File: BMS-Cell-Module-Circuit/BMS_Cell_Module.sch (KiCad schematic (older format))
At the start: 46 parts, among them J1 Conn_01x04_Female, J2 Conn_01x04_Female, J3 Conn_01x02_Male, M1 SI2312BDS-T1-E3, U1 MCP1703A-3302_SOT223, U2 ADUM1250ARZ, U3 ATTINY85-20SU

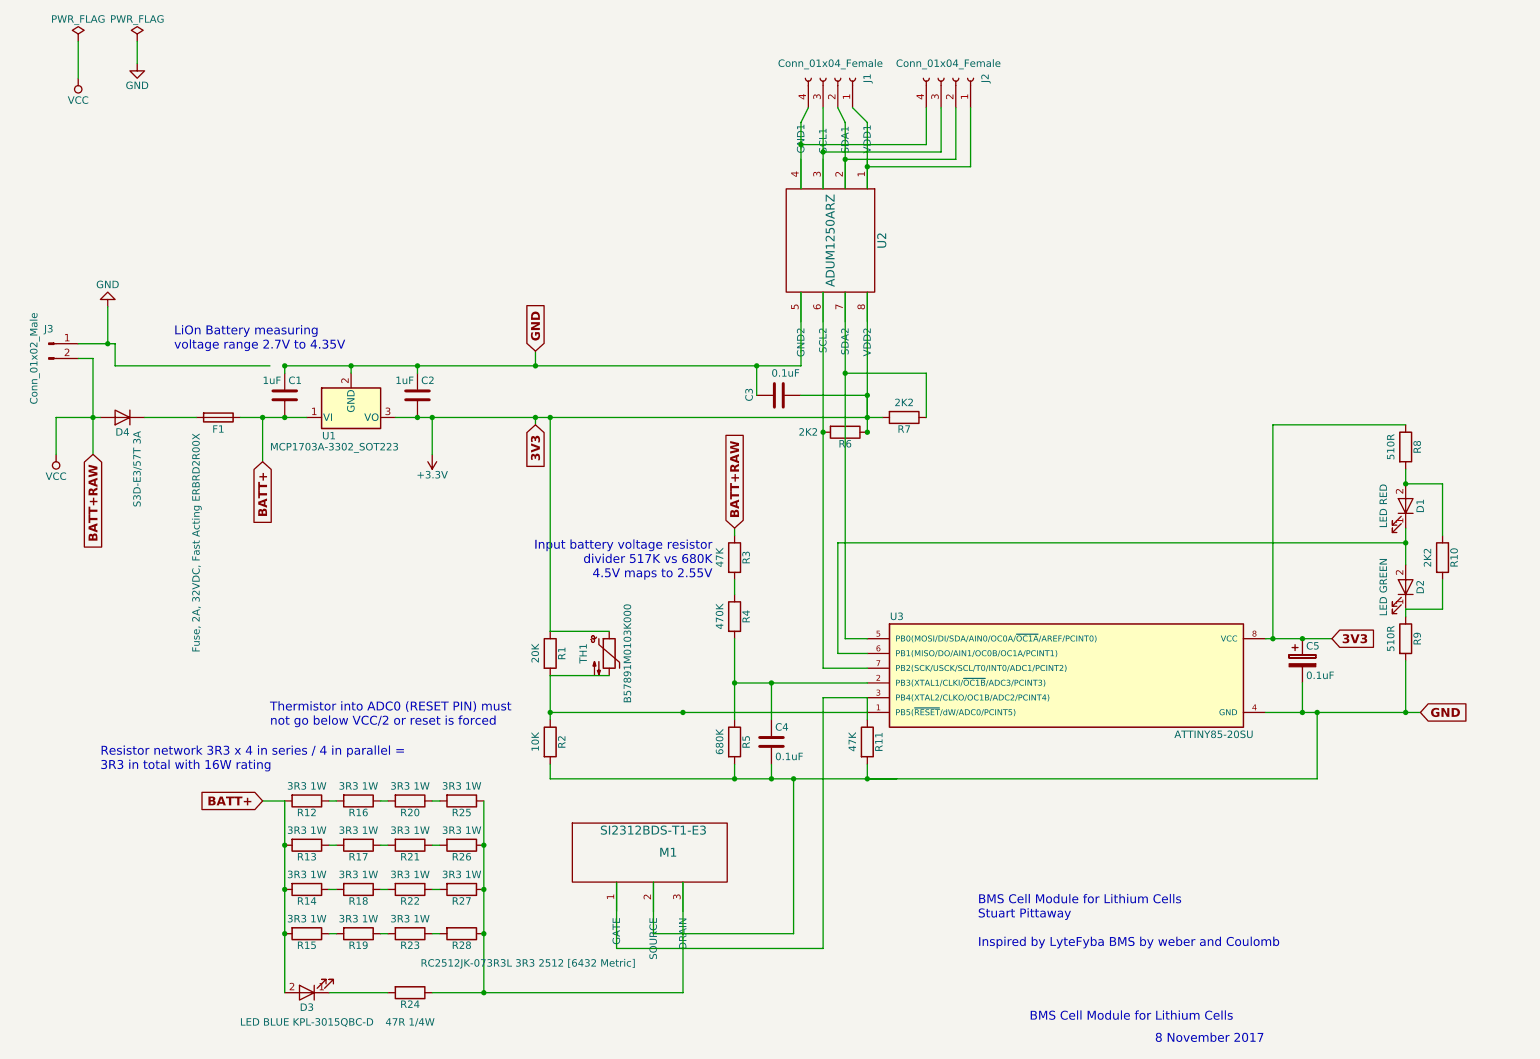
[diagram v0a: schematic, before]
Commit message: Started work on PCB
DONT USE THIS PCB FOR PRODUCTION!
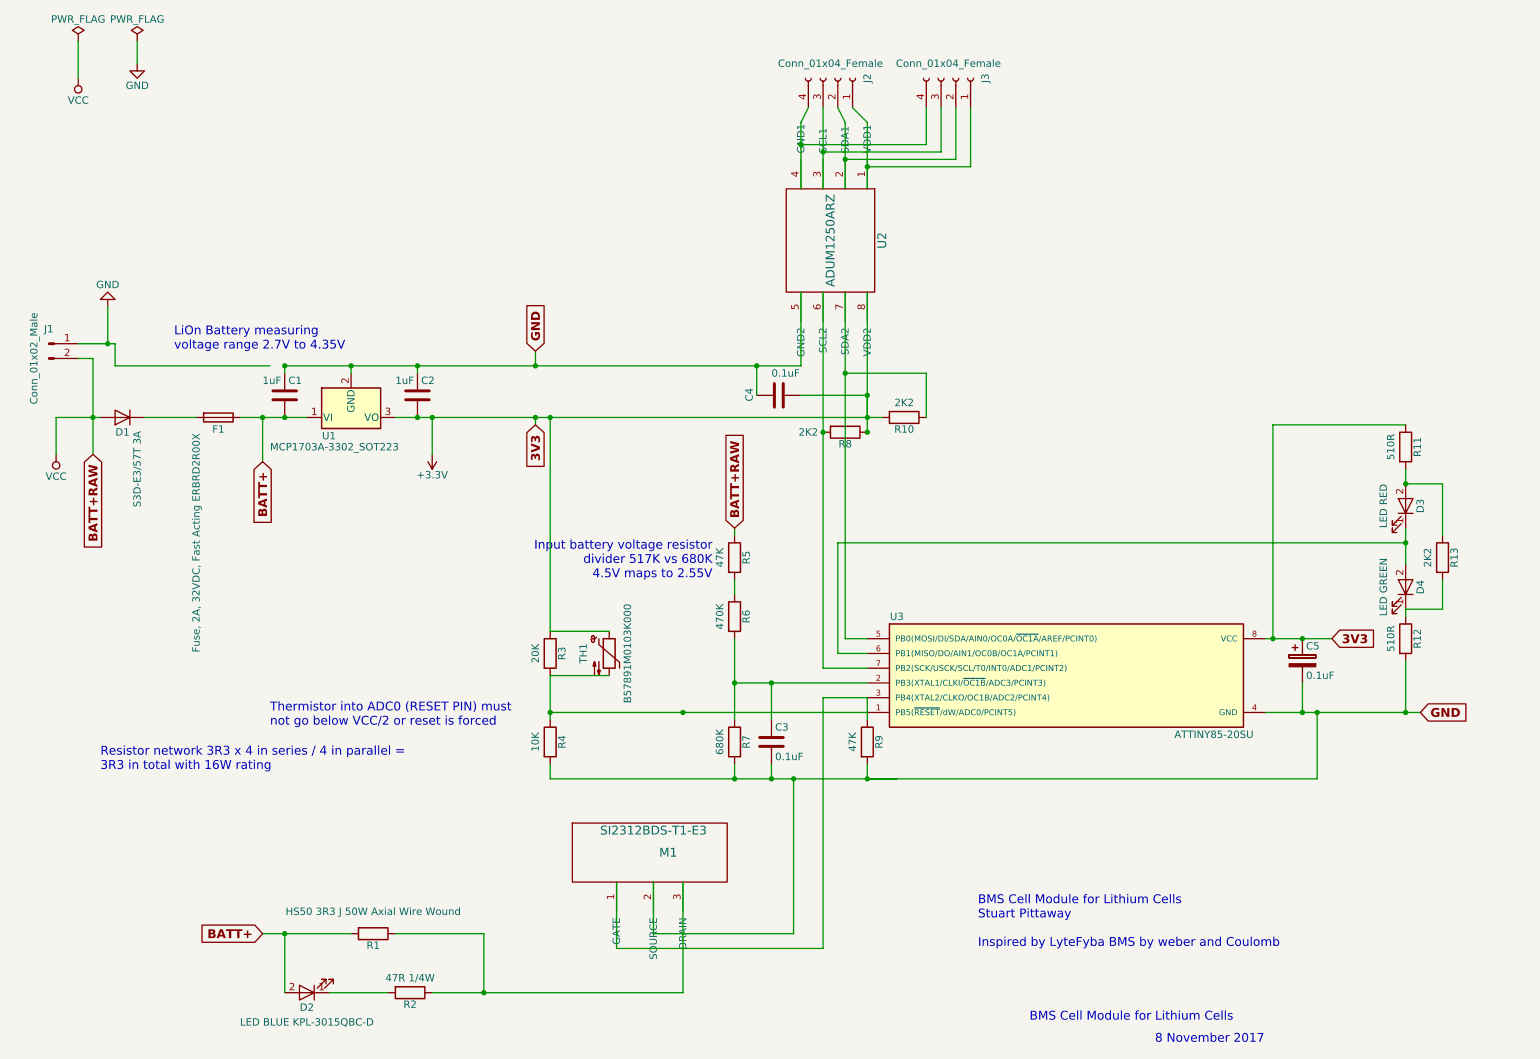
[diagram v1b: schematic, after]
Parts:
- removed R12, R13, R14, R15, R16, R17, R18, R19, R20, R21, R22, R23, R25, R26, R27: 3R3 1W, Resistors_SMD:R_2512_HandSoldering, symbol R
- removed R28: RC2512JK-073R3L 3R3 2512 [6432 Metric], Resistors_SMD:R_2512_HandSoldering, symbol R
- added R1: HS50 3R3 J 50W Axial Wire Wound, Resistors_THT:R_Axial_Power_L60.0mm_W14.0mm_P71.12mm, symbol R
- TH1: footprint Pin_Headers:Pin_Header_Straight_1x02_Pitch2.54mm -> Resistors_THT:R_Axial_DIN0204_L3.6mm_D1.6mm_P2.54mm_Vertical
- renumbered C4 to C3, C3 to C4, D4 to D1, D3 to D2, D1 to D3, D2 to D4, J3 to J1, J1 to J2, J2 to J3, R7 to R10, R8 to R11, R9 to R12, R10 to R13, R24 to R2, R1 to R3, R2 to R4, R3 to R5, R4 to R6, R5 to R7, R6 to R8, R11 to R9
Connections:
- net BATT+: now also R1.2
- net at M1.3 (DRAIN), R2.1: now also R1.1

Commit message: Split board into two sections
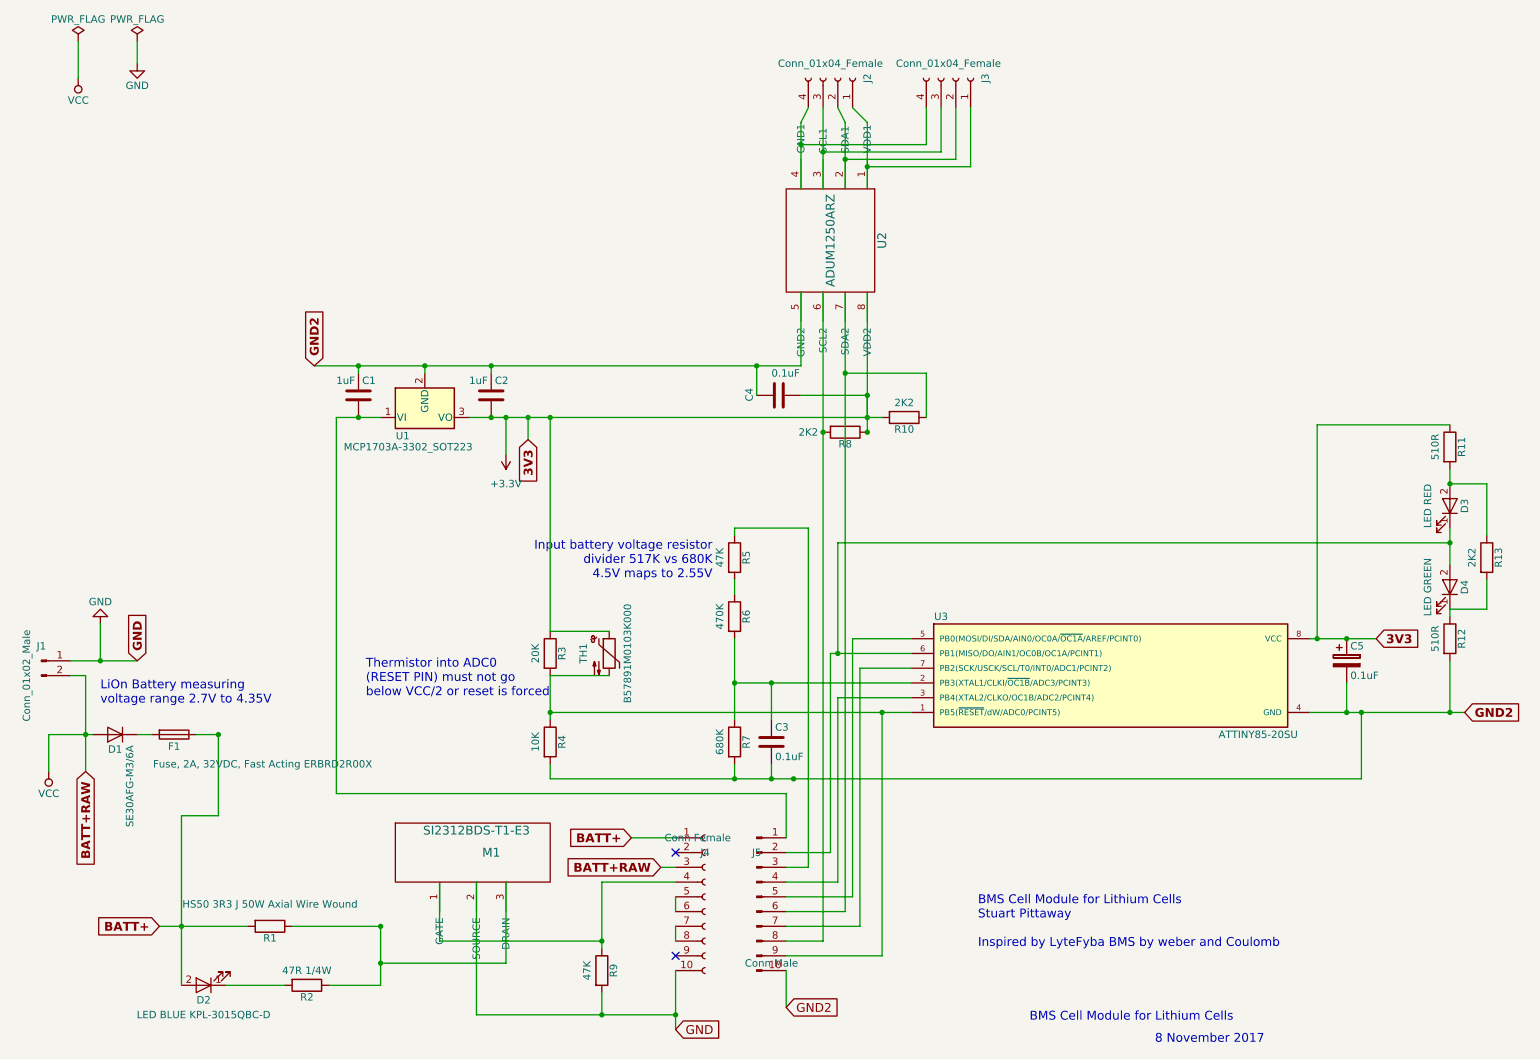
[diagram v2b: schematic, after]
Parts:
- added J4: Conn Female, Socket_Strips:Socket_Strip_Angled_1x10_Pitch2.54mm, symbol Conn_01x10_Female
- added J5: Conn Male, Pin_Headers:Pin_Header_Angled_1x10_Pitch2.54mm, symbol Conn_01x10_Male
- D1: value S3D-E3/57T 3A -> SE30AFG-M3/6A; footprint Diodes_SMD:D_SMC_Handsoldering -> Diodes_SMD:D_SMA
- D2, D3, D4: footprint LEDs:LED_0603_HandSoldering -> LEDs:LED_1206_HandSoldering
- J1: footprint Connectors_JST:JST_VH_B2PS-VH_2x2x3.96mm_Horizontal -> Connectors_JST:JST_EH_S02B-EH_02x2.50mm_Angled
- R1: footprint Resistors_THT:R_Axial_Power_L60.0mm_W14.0mm_P71.12mm -> Resistors_THT:R_Axial_Power_L50.0mm_W9.0mm_P60.96mm
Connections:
- net BATT+: now also J4.1 (Pin_1); no longer C1.2, U1.1 (VI)
- net GND: now also J4.10 (Pin_10); no longer C1.1, C2.1, C3.2, C4.2, C5.2, R12.2, R4.2, R7.2, U1.2 (GND), U2.5 (GND2), U3.4 (GND)
- net VCC: now also J4.3 (Pin_3); no longer R5.1
- net at R3.2, R4.1, TH1.2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: now also J5.9 (Pin_9)
- net at M1.1 (GATE), R9.1: now also J4.4 (Pin_4); no longer U3.3 (PB4(XTAL2/CLKO/OC1B/ADC2/PCINT4))
- net at R10.1, U2.7 (SDA2): now also J5.6 (Pin_6); no longer U3.5 (PB0(MOSI/DI/SDA/AIN0/OC0A/~OC1A~/AREF/PCINT0))
- net at D3.1 (K), D4.2 (A), U3.6 (PB1(MISO/DO/AIN1/OC0B/OC1A/PCINT1)): now also J5.2 (Pin_2)
- net at R8.2, U2.6 (SCL2): now also J5.8 (Pin_8); no longer U3.7 (PB2(SCK/USCK/SCL/T0/INT0/ADC1/PCINT2))
- new net: J5.4 (Pin_4), U3.3 (PB4(XTAL2/CLKO/OC1B/ADC2/PCINT4))
- new net: J5.5 (Pin_5), U3.5 (PB0(MOSI/DI/SDA/AIN0/OC0A/~OC1A~/AREF/PCINT0))
- new net: J5.7 (Pin_7), U3.7 (PB2(SCK/USCK/SCL/T0/INT0/ADC1/PCINT2))
- new net: C1.2, J5.1 (Pin_1), U1.1 (VI)
- new net: J5.3 (Pin_3), R5.1
- new net: J4.5 (Pin_5), J4.6 (Pin_6)
- new net: J4.7 (Pin_7), J4.8 (Pin_8)
- new net GND2: C1.1, C2.1, C3.2, C4.2, C5.2, J5.10 (Pin_10), R12.2, R4.2, R7.2, U1.2 (GND), U2.5 (GND2), U3.4 (GND)
- no-connect marks 0 -> 2
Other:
- note added: "Thermistor into ADC0 \n(RESET PIN) must not go \nbelow VCC/2 or reset is forced"
- note removed: "Resistor network 3R3 x 4 in series / 4 in parallel = \n3R3 in total with 16W rating"
- note removed: "Thermistor into ADC0 (RESET PIN) must \nnot go below VCC/2 or reset is forced"
- moved on the sheet: C1, C2, C5, D1, D2, D3, D4, F1, J1, M1, R1, R11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

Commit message: All pins connected on PCB
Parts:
- added TP1: TEST, Connectors:PINTST, symbol TEST
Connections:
- net at C3.1, R6.2, R7.1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: now also TP1.1
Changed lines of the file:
@@
 $EndComp
 $Comp
-L GND #PWR01
+L GND #PWR3
 U 1 1 5A022A52
 P 1150 4800
-F 0 "#PWR01" H 1150 4550 50  0001 C CNN
+F 0 "#PWR3" H 1150 4550 50  0001 C CNN
 F 1 "GND" H 1150 4650 50  0000 C CNN
 F 2 "" H 1150 4800 50  0001 C CNN
@@
 $EndComp
 $Comp
-L +3.3V #PWR02
+L +3.3V #PWR5
 U 1 1 5A022FFB
 P 3900 3650
-F 0 "#PWR02" H 3900 3500 50  0001 C CNN
+F 0 "#PWR5" H 3900 3500 50  0001 C CNN
 F 1 "+3.3V" H 3900 3850 50  0000 C CNN
 F 2 "" H 3900 3650 50  0001 C CNN
@@
 $EndComp
 $Comp
-L PWR_FLAG #FLG03
+L PWR_FLAG #FLG1
 U 1 1 5A024000
 P 1000 850
-F 0 "#FLG03" H 1000 925 50  0001 C CNN
+F 0 "#FLG1" H 1000 925 50  0001 C CNN
 F 1 "PWR_FLAG" H 1000 1000 50  0000 C CNN
 F 2 "" H 1000 850 50  0001 C CNN
@@
 $EndComp
 $Comp
-L PWR_FLAG #FLG04
+L PWR_FLAG #FLG2
 U 1 1 5A02407E
 P 1400 850
-F 0 "#FLG04" H 1400 925 50  0001 C CNN
+F 0 "#FLG2" H 1400 925 50  0001 C CNN
 F 1 "PWR_FLAG" H 1400 1000 50  0000 C CNN
 F 2 "" H 1400 850 50  0001 C CNN
@@
 $EndComp
 $Comp
-L VCC #PWR05
+L VCC #PWR2
 U 1 1 5A0240F2
 P 1000 1100
-F 0 "#PWR05" H 1000 950 50  0001 C CNN
+F 0 "#PWR2" H 1000 950 50  0001 C CNN
 F 1 "VCC" H 1000 1250 50  0000 C CNN
 F 2 "" H 1000 1100 50  0001 C CNN
@@
 $EndComp
 $Comp
-L GND #PWR06
+L GND #PWR4
 U 1 1 5A024136
 P 1400 1000
-F 0 "#PWR06" H 1400 750 50  0001 C CNN
+F 0 "#PWR4" H 1400 750 50  0001 C CNN
 F 1 "GND" H 1400 850 50  0000 C CNN
 F 2 "" H 1400 1000 50  0001 C CNN
@@
 $EndComp
 $Comp
-L VCC #PWR07
+L VCC #PWR1
 U 1 1 5A04296E
 P 800 5800
-F 0 "#PWR07" H 800 5650 50  0001 C CNN
+F 0 "#PWR1" H 800 5650 50  0001 C CNN
 F 1 "VCC" H 800 5950 50  0000 C CNN
 F 2 "" H 800 5800 50  0001 C CNN
@@
 	2600 3050 5900 3050
 Wire Wire Line
-	5450 5200 6650 5200
+	5150 5200 6650 5200
 Wire Wire Line
 	1150 4800 1150 5050
@@
 	4550 7300 4550 7450
 Connection ~ 4550 7450
+$Comp
+L TEST TP1
+U 1 1 5A0A2523
+P 5150 5200
+F 0 "TP1" H 5150 5500 50  0000 C BNN
+F 1 "TEST" H 5150 5450 50  0000 C CNN
+F 2 "Connectors:PINTST" H 5150 5200 50  0001 C CNN
+F 3 "" H 5150 5200 50  0001 C CNN
+	1    5150 5200
+	1    0    0    -1
+$EndComp
 $EndSCHEMATC

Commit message: Added ground plane to pcb
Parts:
- F1: value Fuse, 2A, 32VDC, Fast Acting ERBRD2R00X -> MC36232 1.5A 24V; footprint Resistors_SMD:R_0402 -> Resistors_SMD:R_1812_HandSoldering
- J1: value Conn_01x02_Male -> Conn_01x02_Female; footprint Connectors_JST:JST_EH_S02B-EH_02x2.50mm_Angled -> Connectors_JST:JST_SFH_SM02B-SFHRS-TF_02x1.80mm_Angled; symbol Conn_01x02_Male -> Conn_01x02_Female
- TP1: value TEST -> VDIV
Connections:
- net GND: now also J1.2 (Pin_2); no longer J1.1 (Pin_1)
- net VCC: now also J1.1 (Pin_1); no longer J1.2 (Pin_2)
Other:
- moved on the sheet: R5, R6
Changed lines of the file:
@@
 L R R6
 U 1 1 5A01000D
-P 5450 4750
-F 0 "R6" V 5530 4750 50  0000 C CNN
-F 1 "470K" V 5350 4750 50  0000 C CNN
-F 2 "Resistors_SMD:R_1206_HandSoldering" V 5380 4750 50  0001 C CNN
-F 3 "" H 5450 4750 50  0001 C CNN
-	1    5450 4750
+P 5450 4900
+F 0 "R6" V 5530 4900 50  0000 C CNN
+F 1 "470K" V 5350 4900 50  0000 C CNN
+F 2 "Resistors_SMD:R_1206_HandSoldering" V 5380 4900 50  0001 C CNN
+F 3 "" H 5450 4900 50  0001 C CNN
+	1    5450 4900
 	1    0    0    -1
 $EndComp
@@
 Text GLabel 10400 5400 2    60   Input ~ 12
 GND2
-Text Notes 5300 4500 2    60   ~ 0
+Text Notes 5750 4450 2    60   ~ 0
 Input battery voltage resistor \ndivider 517K vs 680K\n4.5V maps to 2.55V
 Text Notes 1150 5350 0    60   ~ 0
@@
 L R R5
 U 1 1 5A011F78
-P 5450 4350
-F 0 "R5" V 5530 4350 50  0000 C CNN
-F 1 "47K" V 5350 4350 50  0000 C CNN
-F 2 "Resistors_SMD:R_1206_HandSoldering" V 5380 4350 50  0001 C CNN
-F 3 "" H 5450 4350 50  0001 C CNN
-	1    5450 4350
+P 5450 4500
+F 0 "R5" V 5530 4500 50  0000 C CNN
+F 1 "47K" V 5350 4500 50  0000 C CNN
+F 2 "Resistors_SMD:R_1206_HandSoldering" V 5380 4500 50  0001 C CNN
+F 3 "" H 5450 4500 50  0001 C CNN
+	1    5450 4500
 	1    0    0    -1
 $EndComp
@@
 $EndComp
 $Comp
-L Conn_01x02_Male J1
+L Conn_01x02_Female J1
 U 1 1 5A0226E7
-P 750 5050
-F 0 "J1" H 750 5150 50  0000 C CNN
-F 1 "Conn_01x02_Male" V 650 4950 50  0000 C CNN
-F 2 "Connectors_JST:JST_EH_S02B-EH_02x2.50mm_Angled" H 750 5050 50  0001 C CNN
-F 3 "" H 750 5050 50  0001 C CNN
-	1    750  5050
-	1    0    0    -1
-$EndComp
-$Comp
-L GND #PWR3
+P 700 5150
+F 0 "J1" H 700 5250 50  0000 C CNN
+F 1 "Conn_01x02_Female" V 800 5050 50  0000 C CNN
+F 2 "Connectors_JST:JST_SFH_SM02B-SFHRS-TF_02x1.80mm_Angled" H 700 5150 50  0001 C CNN
+F 3 "" H 700 5150 50  0001 C CNN
+	1    700  5150
+	-1   0    0    1
+$EndComp
+$Comp
+L GND #PWR01
 U 1 1 5A022A52
 P 1150 4800
-F 0 "#PWR3" H 1150 4550 50  0001 C CNN
+F 0 "#PWR01" H 1150 4550 50  0001 C CNN
 F 1 "GND" H 1150 4650 50  0000 C CNN
 F 2 "" H 1150 4800 50  0001 C CNN
@@
 $EndComp
 $Comp
-L +3.3V #PWR5
+L +3.3V #PWR02
 U 1 1 5A022FFB
 P 3900 3650
-F 0 "#PWR5" H 3900 3500 50  0001 C CNN
+F 0 "#PWR02" H 3900 3500 50  0001 C CNN
 F 1 "+3.3V" H 3900 3850 50  0000 C CNN
 F 2 "" H 3900 3650 50  0001 C CNN
@@
 $EndComp
 $Comp
-L PWR_FLAG #FLG1
+L PWR_FLAG #FLG03
 U 1 1 5A024000
 P 1000 850
-F 0 "#FLG1" H 1000 925 50  0001 C CNN
+F 0 "#FLG03" H 1000 925 50  0001 C CNN
 F 1 "PWR_FLAG" H 1000 1000 50  0000 C CNN
 F 2 "" H 1000 850 50  0001 C CNN
@@
 $EndComp
 $Comp
-L PWR_FLAG #FLG2
+L PWR_FLAG #FLG04
 U 1 1 5A02407E
 P 1400 850
-F 0 "#FLG2" H 1400 925 50  0001 C CNN
+F 0 "#FLG04" H 1400 925 50  0001 C CNN
 F 1 "PWR_FLAG" H 1400 1000 50  0000 C CNN
 F 2 "" H 1400 850 50  0001 C CNN
@@
 $EndComp
 $Comp
-L VCC #PWR2
+L VCC #PWR05
 U 1 1 5A0240F2
 P 1000 1100
-F 0 "#PWR2" H 1000 950 50  0001 C CNN
+F 0 "#PWR05" H 1000 950 50  0001 C CNN
 F 1 "VCC" H 1000 1250 50  0000 C CNN
 F 2 "" H 1000 1100 50  0001 C CNN
@@
 $EndComp
 $Comp
-L GND #PWR4
+L GND #PWR06
 U 1 1 5A024136
 P 1400 1000
-F 0 "#PWR4" H 1400 750 50  0001 C CNN
+F 0 "#PWR06" H 1400 750 50  0001 C CNN
 F 1 "GND" H 1400 850 50  0000 C CNN
 F 2 "" H 1400 1000 50  0001 C CNN
@@
 $EndComp
 $Comp
-L VCC #PWR1
+L VCC #PWR07
 U 1 1 5A04296E
 P 800 5800
-F 0 "#PWR1" H 800 5650 50  0001 C CNN
+F 0 "#PWR07" H 800 5650 50  0001 C CNN
 F 1 "VCC" H 800 5950 50  0000 C CNN
 F 2 "" H 800 5800 50  0001 C CNN
@@
 P 1650 5550
 F 0 "F1" V 1730 5550 50  0000 C CNN
-F 1 "Fuse, 2A, 32VDC, Fast Acting ERBRD2R00X" V 1850 6150 50  0000 C CNN
-F 2 "Resistors_SMD:R_0402" V 1580 5550 50  0001 C CNN
-F 3 "http://www.farnell.com/datasheets/2244247.pdf" H 1650 5550 50  0001 C CNN
+F 1 "MC36232 1.5A 24V" V 1850 6150 50  0000 C CNN
+F 2 "Resistors_SMD:R_1812_HandSoldering" V 1580 5550 50  0001 C CNN
+F 3 "http://uk.farnell.com/multicomp/mc36232/fuse-ptc-reset-smd-24v-1-5a/dp/1861171" H 1650 5550 50  0001 C CNN
 	1    1650 5550
 	0    1    1    0
@@
 Connection ~ 9600 4900
 Wire Wire Line
-	5700 5450 5700 5200
+	5700 5200 5700 5450
 Connection ~ 5700 5200
 Wire Wire Line
@@
 Connection ~ 9700 5400
 Wire Wire Line
-	5450 4900 5450 5450
+	5450 5050 5450 5450
 Wire Wire Line
 	5450 5750 5450 5850
@@
 Connection ~ 5450 5200
 Wire Wire Line
-	5450 4500 5450 4600
+	5450 4650 5450 4750
 Wire Wire Line
 	4200 4850 4600 4850
@@
 	2900 3050 2900 3100
 Wire Wire Line
-	5450 4150 5450 4200
+	5450 4300 5450 4350
 Wire Wire Line
 	5950 1300 5900 1400
@@
 Connection ~ 5900 1550
 Wire Wire Line
-	950  5150 1050 5150
-Wire Wire Line
-	1050 5150 1050 5800
+	900  5050 1150 5050
 Connection ~ 1050 5550
 Connection ~ 1150 5050
@@
 Connection ~ 1950 5550
 Wire Wire Line
-	950  5050 1400 5050
-Wire Wire Line
 	2750 3400 3050 3400
 Wire Wire Line
@@
 	5150 5200 6650 5200
 Wire Wire Line
-	1150 4800 1150 5050
+	1150 5050 1150 4800
 Wire Wire Line
 	1800 5550 1950 5550
@@
 Connection ~ 3050 6850
 Wire Wire Line
-	5450 4150 5950 4150
-Wire Wire Line
-	5950 4150 5950 6450
+	5450 4300 5950 4300
+Wire Wire Line
+	5950 4300 5950 6450
 Wire Wire Line
 	5950 6450 5800 6450
 Text GLabel 4950 6450 0    60   Input ~ 12
 BATT+RAW
-Wire Wire Line
-	4950 6450 5050 6450
 Wire Wire Line
 	2750 3400 2750 5950
@@
 P 5150 5200
 F 0 "TP1" H 5150 5500 50  0000 C BNN
-F 1 "TEST" H 5150 5450 50  0000 C CNN
+F 1 "VDIV" H 5150 5450 50  0000 C CNN
 F 2 "Connectors:PINTST" H 5150 5200 50  0001 C CNN
 F 3 "" H 5150 5200 50  0001 C CNN
@@
 	1    0    0    -1
 $EndComp
+Wire Wire Line
+	900  5150 1050 5250
+Wire Wire Line
+	1050 5250 1050 5800
+Wire Wire Line
+	5050 6450 4950 6450
 $EndSCHEMATC
